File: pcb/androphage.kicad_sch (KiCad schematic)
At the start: 0 parts

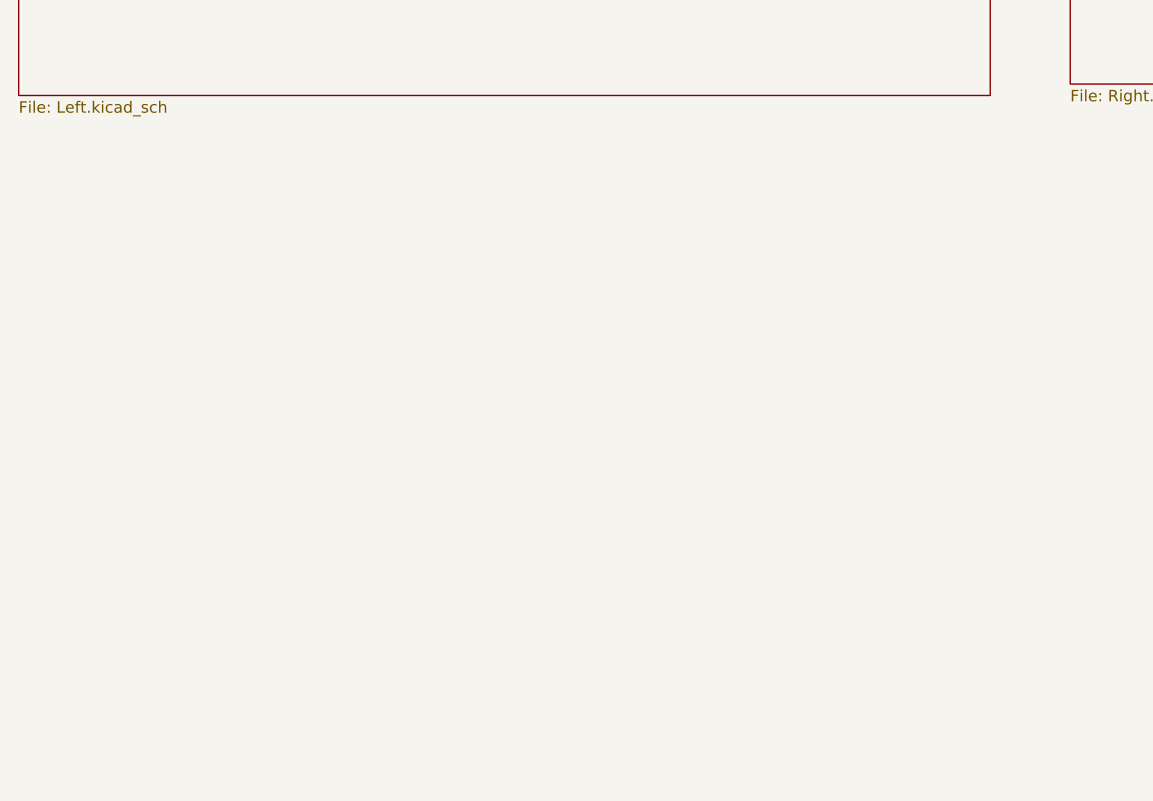
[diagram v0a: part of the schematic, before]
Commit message: Create VIK hat for Seeed Xiao nRF.
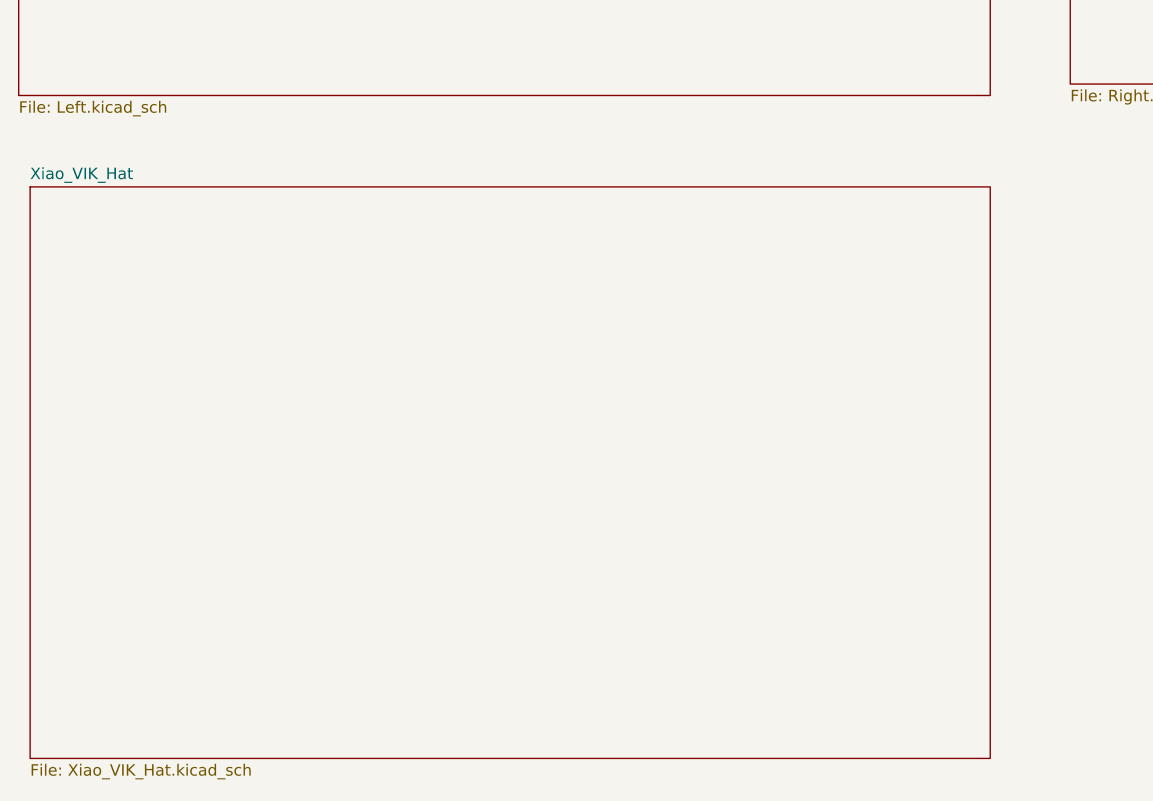
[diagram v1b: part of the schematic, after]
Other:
- added sheet Xiao_VIK_Hat (Xiao_VIK_Hat.kicad_sch)
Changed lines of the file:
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@@
 		)
 		(instances
-			(project "unikyria"
+			(project "androphage"
 				(path "/75763295-000b-439c-b3ba-6692a992e76d"
 					(page "2")
@@
 		)
 		(instances
-			(project "unikyria"
+			(project "androphage"
 				(path "/75763295-000b-439c-b3ba-6692a992e76d"
 					(page "3")
 				)
 			)
+		)
+	)
+	(sheet
+		(at 5.08 90.17)
+		(size 106.68 63.5)
+		(exclude_from_sim no)
+		(in_bom yes)
+		(on_board yes)
+		(dnp no)
+		(fields_autoplaced yes)
+		(stroke
+			(width 0.1524)
+			(type solid)
+		)
+		(fill
+			(color 0 0 0 0.0000)
+		)
+		(property "Sheetname" "Xiao_VIK_Hat"
+			(at 5.08 89.4584 0)
+			(effects
+				(font
+					(size 1.27 1.27)
+				)
+				(justify left bottom)
+			)
+		)
+		(property "Sheetfile" "Xiao_VIK_Hat.kicad_sch"
+			(at 5.08 154.2546 0)
+			(effects
+				(font
+					(size 1.27 1.27)
+				)
+				(justify left top)
+			)
+		)
+		(property "Field2" ""
+			(at 5.08 90.17 0)
+			(effects
+				(font
+					(size 1.27 1.27)
+				)
+			)
+		)
+		(instances
+			(project "androphage"
+				(path "/75763295-000b-439c-b3ba-6692a992e76d"
+					(page "4")
+				)
+			)

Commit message: Tentatively finish PCB design.
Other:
- removed sheet Left
- removed sheet Right
- removed sheet Xiao_VIK_Hat
- added sheet Left_Switches (Left_Switches.kicad_sch)
- added sheet Right_Switches (Right_Switches.kicad_sch)
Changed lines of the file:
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@@
 	(paper "A4")
 	(sheet
-		(at 3.81 3.81)
-		(size 107.95 76.2)
+		(at 130.81 16.51)
+		(size 115.57 82.55)
 		(exclude_from_sim no)
 		(in_bom yes)
@@
 			(color 0 0 0 0.0000)
 		)
-		(property "Sheetname" "Left"
-			(at 3.81 3.0984 0)
+		(property "Sheetname" "Right_Switches"
+			(at 130.81 15.7984 0)
 			(effects
 				(font
@@
 			)
 		)
-		(property "Sheetfile" "Left.kicad_sch"
-			(at 3.81 80.5946 0)
+		(property "Sheetfile" "Right_Switches.kicad_sch"
+			(at 130.81 99.6446 0)
 			(effects
 				(font
@@
 			(project "androphage"
 				(path "/75763295-000b-439c-b3ba-6692a992e76d"
-					(page "2")
+					(page "5")
 				)
 			)
@@
 	)
 	(sheet
-		(at 120.65 3.81)
-		(size 115.57 74.93)
+		(at 16.51 16.51)
+		(size 106.68 82.55)
 		(exclude_from_sim no)
 		(in_bom yes)
@@
 			(color 0 0 0 0.0000)
 		)
-		(property "Sheetname" "Right"
-			(at 120.65 3.0984 0)
+		(property "Sheetname" "Left_Switches"
+			(at 16.51 15.7984 0)
 			(effects
 				(font
@@
 			)
 		)
-		(property "Sheetfile" "Right.kicad_sch"
-			(at 120.65 79.3246 0)
+		(property "Sheetfile" "Left_Switches.kicad_sch"
+			(at 16.51 99.6446 0)
 			(effects
 				(font
@@
 			)
 		)
-		(property "Field2" ""
-			(at 120.65 3.81 0)
-			(effects
-				(font
-					(size 1.27 1.27)
-				)
-			)
-		)
-		(instances
-			(project "androphage"
-				(path "/75763295-000b-439c-b3ba-6692a992e76d"
-					(page "3")
-				)
-			)
-		)
-	)
-	(sheet
-		(at 5.08 90.17)
-		(size 106.68 63.5)
-		(exclude_from_sim no)
-		(in_bom yes)
-		(on_board yes)
-		(dnp no)
-		(fields_autoplaced yes)
-		(stroke
-			(width 0.1524)
-			(type solid)
-		)
-		(fill
-			(color 0 0 0 0.0000)
-		)
-		(property "Sheetname" "Xiao_VIK_Hat"
-			(at 5.08 89.4584 0)
-			(effects
-				(font
-					(size 1.27 1.27)
-				)
-				(justify left bottom)
-			)
-		)
-		(property "Sheetfile" "Xiao_VIK_Hat.kicad_sch"
-			(at 5.08 154.2546 0)
-			(effects
-				(font
-					(size 1.27 1.27)
-				)
-				(justify left top)
-			)
-		)
-		(property "Field2" ""
-			(at 5.08 90.17 0)
-			(effects
-				(font
-					(size 1.27 1.27)
-				)
-			)
-		)
